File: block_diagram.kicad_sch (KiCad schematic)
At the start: 0 parts

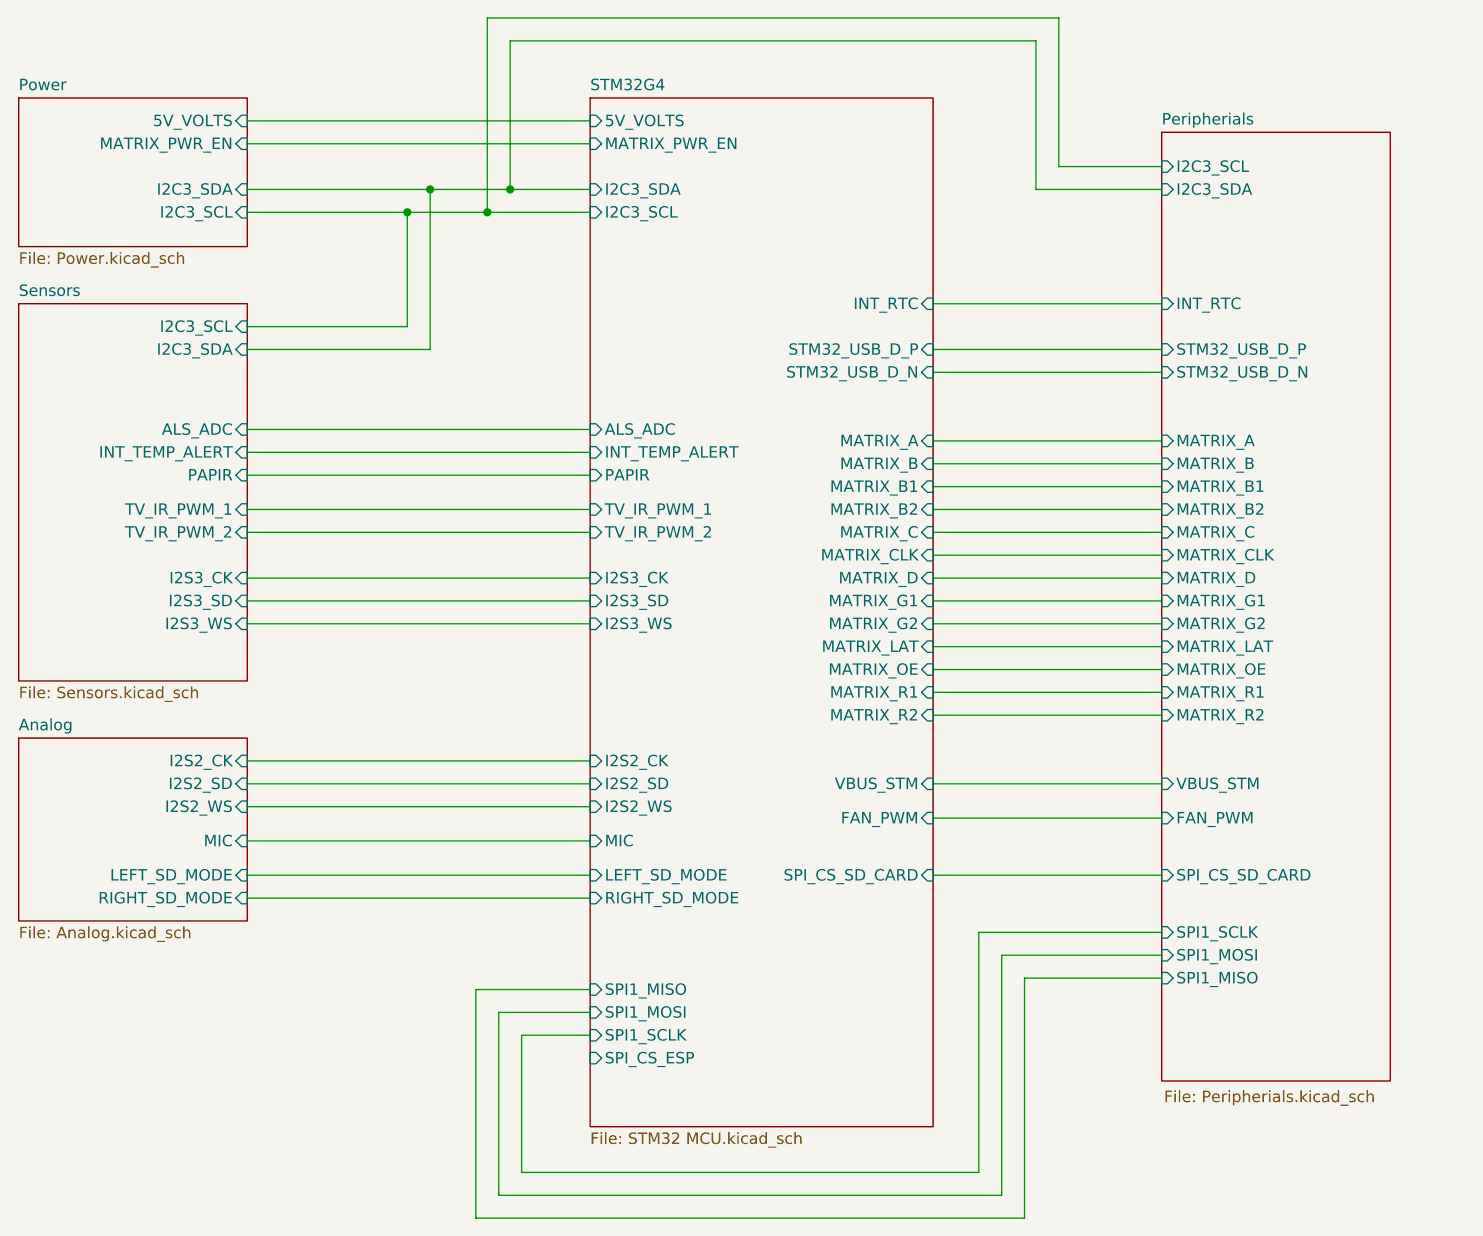
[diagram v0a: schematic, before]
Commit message: got rid of pins on stm32
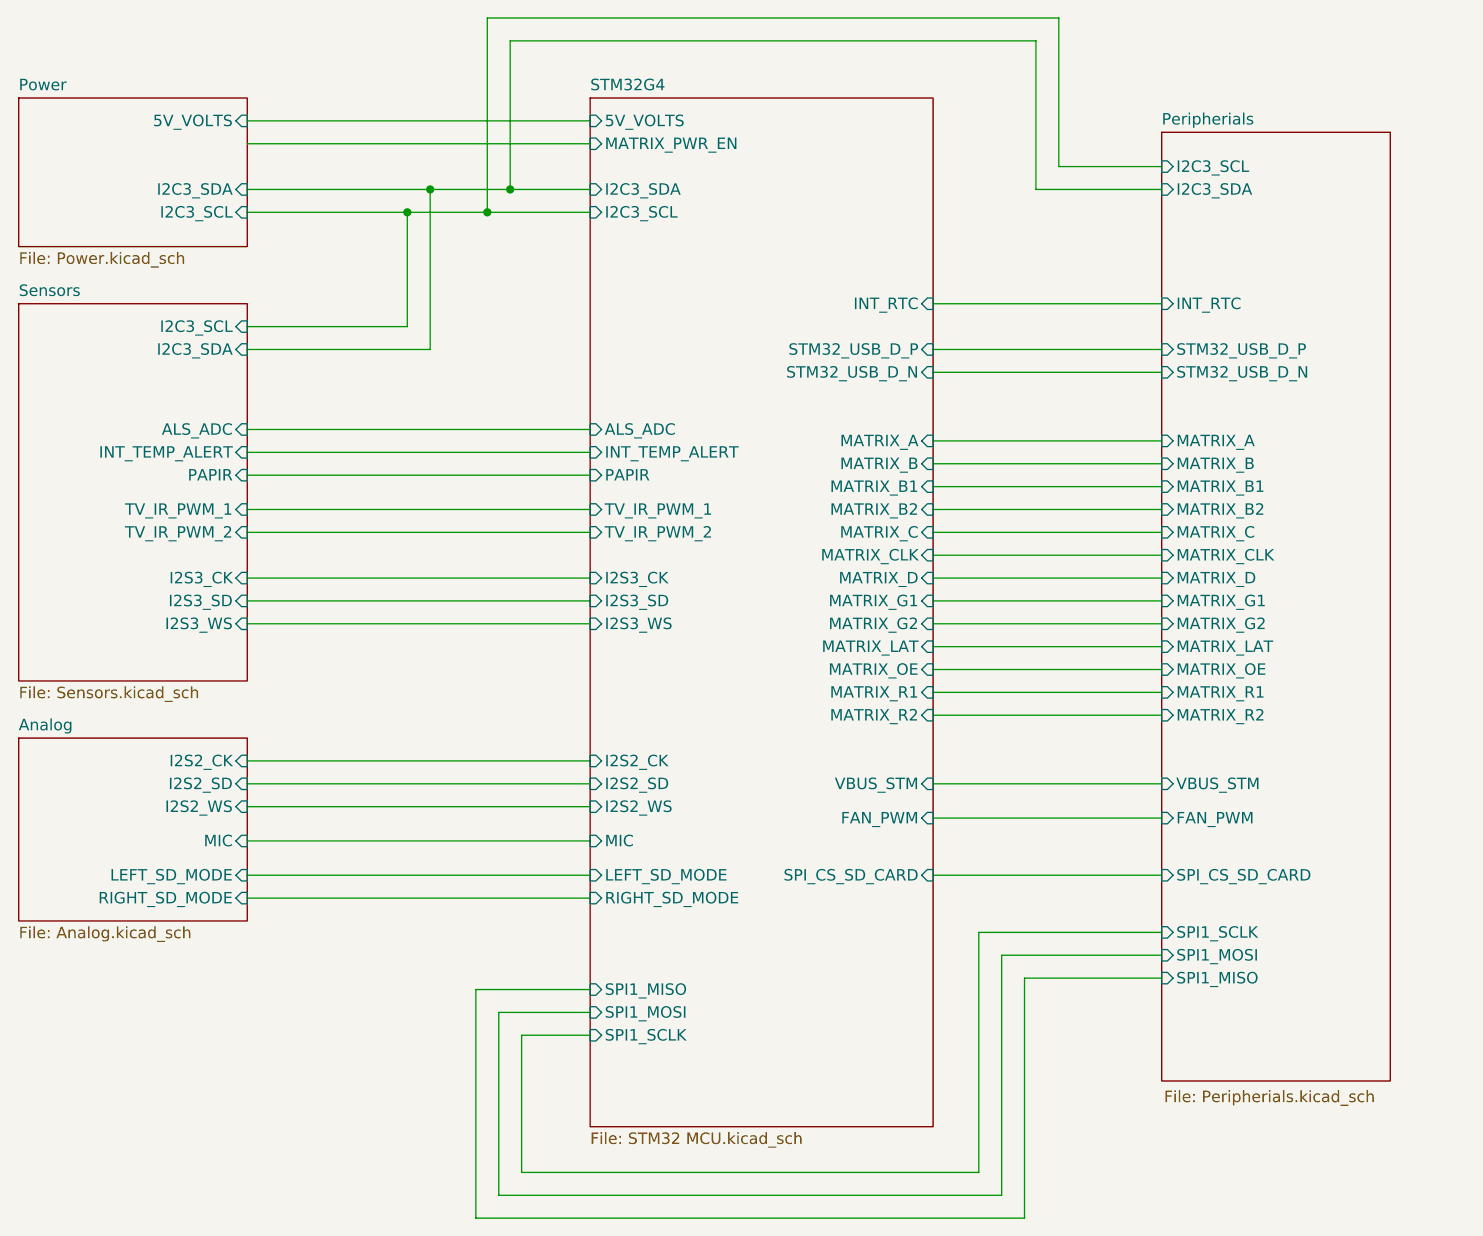
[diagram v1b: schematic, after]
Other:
- sheet Power ports: added none; removed MATRIX_PWR_EN
- sheet STM32G4 ports: added none; removed SPI_CS_ESP
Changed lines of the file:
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@@
-			)
-		)
-		(pin "SPI_CS_ESP" input
-			(at 125.73 132.08 180)
-			(effects
-				(font
-					(size 1.27 1.27)
-				)
-				(justify left)
 			)
 		)
@@
 			(effects
 				(font
-					(size 1.27 1.27)
-				)
-				(justify right)
-			)
-		)
-		(pin "MATRIX_PWR_EN" input
-			(at 87.63 30.48 0)
-			(effects
-				(font
